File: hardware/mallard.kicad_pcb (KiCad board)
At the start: 4 copper layers, 101.6 x 101.6 mm, 75 parts, among them J1 USB_A, J2 Conn_02x03_Odd_Even, J3 Conn_01x03, SW1 RESET Switch, U1 TMP235, U10 LTC1983ES6-3, U11 STM32L4Q5xx, U2 TMP235, U3 TMP235, U4 BQ24210DQCT, U5 TMUX1309, U6 TMUX1309, U7 LMP7721, U8 TPS71710DRVR, U9 LMV554

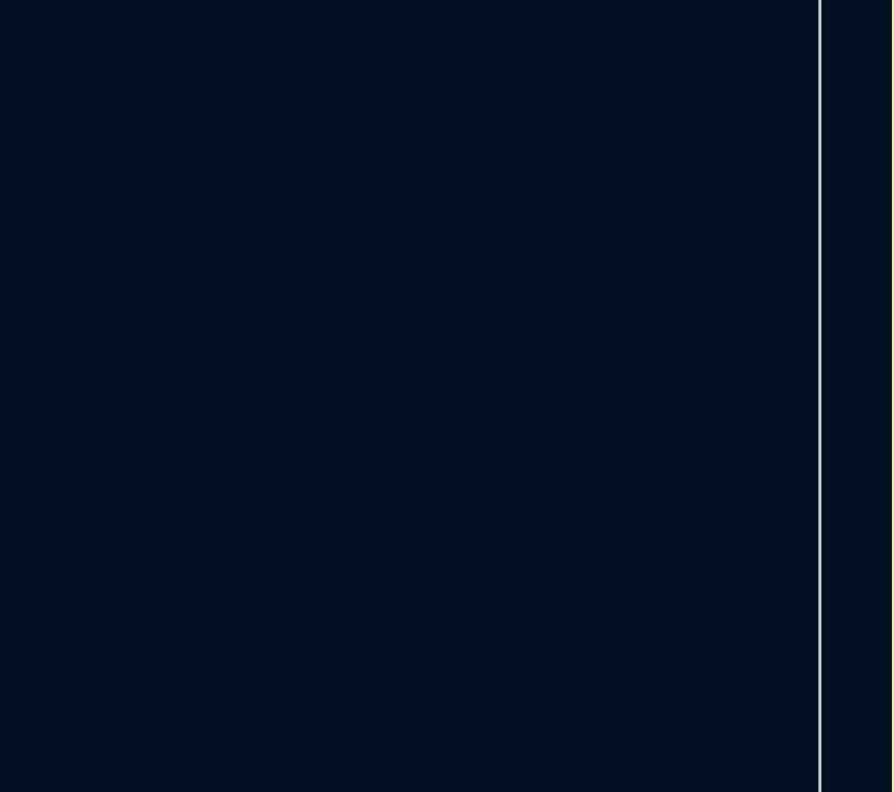
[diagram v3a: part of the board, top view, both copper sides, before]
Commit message: Modified footprints and added items to BOM
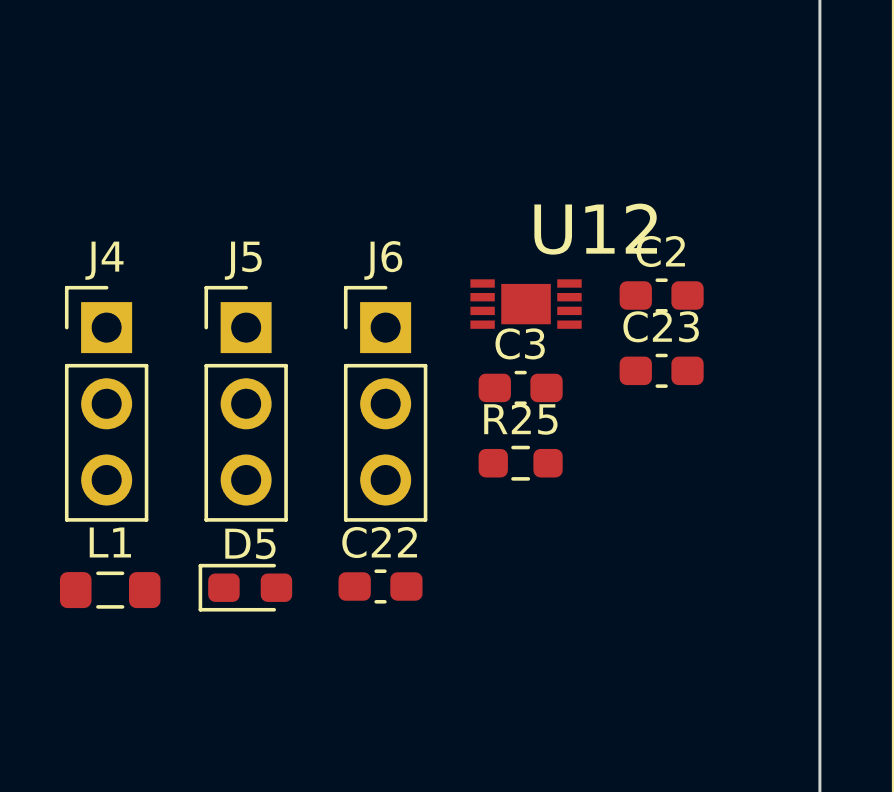
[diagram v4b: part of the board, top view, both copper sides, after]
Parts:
- added C2: 1uF, Capacitor_SMD:C_0603_1608Metric_Pad1.08x0.95mm_HandSolder, F.Cu at (34.9, 78.7)
- added C22: 3.3uF, Capacitor_SMD:C_0603_1608Metric_Pad1.08x0.95mm_HandSolder, F.Cu at (25.6, 88.4)
- added C23: 10uF, Capacitor_SMD:C_0603_1608Metric_Pad1.08x0.95mm_HandSolder, F.Cu at (34.9, 81.2)
- added C3: 1uF, Capacitor_SMD:C_0603_1608Metric_Pad1.08x0.95mm_HandSolder, F.Cu at (30.2, 81.8)
- added D5: RED, LED_SMD:LED_0603_1608Metric_Pad1.05x0.95mm_HandSolder, F.Cu at (21.2, 88.5)
- added J4: Conn_01x03, Connector_PinHeader_2.54mm:PinHeader_1x03_P2.54mm_Vertical, F.Cu at (16.4, 79.8)
- added J5: Conn_01x03, Connector_PinHeader_2.54mm:PinHeader_1x03_P2.54mm_Vertical, F.Cu at (21.1, 79.8)
- added J6: Conn_01x03, Connector_PinHeader_2.54mm:PinHeader_1x03_P2.54mm_Vertical, F.Cu at (25.7, 79.8)
- added L1: 4.7uH, Inductor_SMD:L_0805_2012Metric_Pad1.05x1.20mm_HandSolder, F.Cu at (16.5, 88.6)
- added R25: 370, Resistor_SMD:R_0603_1608Metric_Pad0.98x0.95mm_HandSolder, F.Cu at (30.2, 84.3)
- added U12: LTC3529EDCB, mallard:DFN200X300X80-9N, F.Cu at (30.4, 79.0)
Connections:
- U1 pad 2: GND -> Net-(U1-Pad2)
- U1 pad 4: +3V3 -> Net-(U1-Pad4)
- U11 pad 26: Net-(U11-Pad26) -> 5V_RST
- U11 pad 27: Net-(U11-Pad27) -> 5V_SHDN_L
- U11 pad 28: Net-(U11-Pad28) -> -3V3_SHDN_L
- U2 pad 2: GND -> Net-(U2-Pad2)
- U2 pad 4: +3V3 -> Net-(U2-Pad4)
- U3 pad 2: GND -> Net-(U3-Pad2)
- U3 pad 4: +3V3 -> Net-(U3-Pad4)
- U6 pad 12: Net-(U1-Pad3) -> Net-(J4-Pad2)
- U6 pad 14: Net-(U2-Pad3) -> Net-(J5-Pad2)
- U6 pad 15: Net-(U3-Pad3) -> Net-(J6-Pad2)

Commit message: Schematic and Layout Finished
Needs review
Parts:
- removed the C2 at (34.9, 78.7)
- removed the C2 at (114.8, 28.3)
- removed the C3 at (30.2, 81.8)
- removed D4: Orange, Resistor_SMD:R_0805_2012Metric_Pad1.20x1.40mm_HandSolder
- removed R10, R19: 20k, Resistor_SMD:R_0201_0603Metric_Pad0.64x0.40mm_HandSolder
- removed R13, R17, R24, R4, R6, R8: 10k, Resistor_SMD:R_0201_0603Metric_Pad0.64x0.40mm_HandSolder
- removed R14: 1k, Resistor_SMD:R_0201_0603Metric_Pad0.64x0.40mm_HandSolder
- removed R15: 30k, Resistor_SMD:R_0201_0603Metric_Pad0.64x0.40mm_HandSolder
- removed R16: 20k DNI, Resistor_SMD:R_0201_0603Metric_Pad0.64x0.40mm_HandSolder
- removed R18: 9.1k, Resistor_SMD:R_0201_0603Metric_Pad0.64x0.40mm_HandSolder
- removed R23: 680, Resistor_SMD:R_0603_1608Metric_Pad0.98x0.95mm_HandSolder
- removed U1, U2, U3: TMP235, Connector_PinHeader_2.54mm:PinHeader_1x05_P2.54mm_Vertical
- added C2: 1uF, Capacitor_SMD:C_0603_1608Metric_Pad1.08x0.95mm_HandSolder, F.Cu at (117.8, 38.1)
- moved J4 113.8 mm to (121.9, 37.2), turned to 90 degrees
- moved J5 96.4 mm to (107.5, 37.0), turned to 90 degrees
- moved J6 78.2 mm to (91.1, 36.9), turned to 90 degrees
- moved D5 73.7 mm to (88.8, 118.0), turned to 180 degrees
- moved L1 72.3 mm to (83.6, 115.7), turned to 180 degrees
- moved R25 71.4 mm to (91.2, 121.5), turned to 90 degrees
- moved C22 70.8 mm to (88.1, 121.6), turned to 270 degrees
- moved U12 67.9 mm to (83.4, 121.5)
- moved C23 59.7 mm to (79.0, 121.5), turned to 270 degrees
- moved C20 36.1 mm to (117.4, 101.0), turned to 0 degrees
- moved C19 29.3 mm to (112.2, 106.6)
- moved C18 25.8 mm to (109.8, 110.2)
- moved C3 11.6 mm to (103.2, 37.8), turned to 270 degrees
- moved C17 11.5 mm to (97.2, 107.8)
- moved C1 11.0 mm to (86.5, 37.6), turned to 270 degrees
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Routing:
- net MUX2_A1: track 0.00 -> 46.9 mm, vias 0 -> 2
- net -3V3_SHDN_L: track 0.00 -> 46.5 mm, vias 0 -> 4
- net /RESET_L: track 0.00 -> 46.4 mm
- net MUX2_A0: track 0.00 -> 45.4 mm, vias 0 -> 2
- net Charge_EN: track 1.38 -> 46.5 mm, vias 1 -> 2
- net Moisture_Sense: track 2.16 -> 46.9 mm, vias 0 -> 4
- net /SWDIO: track 0.00 -> 43.9 mm, vias 0 -> 2
- net /SWCLK: track 0.00 -> 42.2 mm, vias 0 -> 2
- net +1V0_EN: track 0.00 -> 42.0 mm, vias 0 -> 2
- net +3V3: track 37.9 -> 79.2 mm, vias 85 -> 90
- net MUX1_A1: track 0.00 -> 40.6 mm, vias 0 -> 2
- net MUX1_A0: track 0.00 -> 40.3 mm, vias 0 -> 2
- net USART1_TX: track 0.00 -> 40.0 mm, vias 0 -> 2
- net MUX1_EN: track 0.00 -> 39.3 mm, vias 0 -> 2
- net MUX2_EN: track 0.00 -> 38.9 mm, vias 0 -> 2
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- added copper zone on F.Cu, net +5V
- added copper zone on Power, net +5V

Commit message: Updated footprints
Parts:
- added C2: 1uF, Capacitor_SMD:C_0603_1608Metric_Pad1.08x0.95mm_HandSolder, F.Cu at (54.0, 20.3)
- added C3: 1uF, Capacitor_SMD:C_0603_1608Metric_Pad1.08x0.95mm_HandSolder, F.Cu at (58.8, 17.4)
- added D4: Orange, Diode_SMD:D_0805_2012Metric_Castellated, F.Cu at (54.2, 17.6)
- added R10: 20k, Resistor_SMD:R_0603_1608Metric_Pad0.98x0.95mm_HandSolder, F.Cu at (54.0, 25.3)
- added R13: 10k, Resistor_SMD:R_0603_1608Metric_Pad0.98x0.95mm_HandSolder, F.Cu at (58.3, 22.8)
- added R14: 1k, Resistor_SMD:R_0603_1608Metric_Pad0.98x0.95mm_HandSolder, F.Cu at (62.7, 19.9)
- added R15: 30k, Resistor_SMD:R_0603_1608Metric_Pad0.98x0.95mm_HandSolder, F.Cu at (67.5, 17.4)
- added R16: 20k DNI, Resistor_SMD:R_0603_1608Metric_Pad0.98x0.95mm_HandSolder, F.Cu at (58.3, 25.3)
- added R17: 10k, Resistor_SMD:R_0603_1608Metric_Pad0.98x0.95mm_HandSolder, F.Cu at (62.7, 22.4)
- added R18: 9.1k, Resistor_SMD:R_0603_1608Metric_Pad0.98x0.95mm_HandSolder, F.Cu at (67.0, 19.9)
- added R19: 20k, Resistor_SMD:R_0603_1608Metric_Pad0.98x0.95mm_HandSolder, F.Cu at (62.7, 24.9)
- added R23: 680, Resistor_SMD:R_0603_1608Metric_Pad0.98x0.95mm_HandSolder, F.Cu at (67.0, 22.4)
- added R24: 10k, Resistor_SMD:R_0603_1608Metric_Pad0.98x0.95mm_HandSolder, F.Cu at (67.0, 24.9)
- added R4: 10k, Resistor_SMD:R_0603_1608Metric_Pad0.98x0.95mm_HandSolder, F.Cu at (54.0, 22.8)
- added R6: 10k, Resistor_SMD:R_0603_1608Metric_Pad0.98x0.95mm_HandSolder, F.Cu at (58.3, 20.3)
- added R8: 10k, Resistor_SMD:R_0603_1608Metric_Pad0.98x0.95mm_HandSolder, F.Cu at (63.2, 17.4)

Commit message: Finished schematic and layout
Needs review
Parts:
- removed the C2 at (54.0, 20.3)
- removed the C3 at (58.8, 17.4)
- moved D4 106.5 mm to (104.0, 111.7), turned to 270 degrees
- moved R24 104.9 mm to (132.4, 106.8), turned to 270 degrees
- moved R23 95.5 mm to (101.2, 111.6), turned to 270 degrees
- moved R15 93.1 mm to (129.7, 86.7), turned to 270 degrees
- moved R16 91.5 mm to (126.2, 86.7), turned to 90 degrees
- moved R14 86.6 mm to (117.8, 86.7), turned to 270 degrees
- moved R17 86.5 mm to (120.5, 86.7), turned to 90 degrees
- moved R13 84.0 mm to (112.9, 86.7), turned to 270 degrees
- moved R18 82.4 mm to (115.3, 86.7), turned to 90 degrees
- moved R10 80.0 mm to (106.7, 85.6), turned to 180 degrees
- moved R19 78.1 mm to (110.5, 86.7), turned to 270 degrees
- moved R8 77.2 mm to (99.5, 85.5), turned to 180 degrees
- moved R6 64.4 mm to (101.5, 68.2), turned to 270 degrees
- moved R4 63.9 mm to (99.0, 68.2), turned to 90 degrees
- moved C5 10.7 mm to (91.7, 57.1)
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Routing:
- net Eh_Sense: track 30.1 -> 41.4 mm, vias 0 -> 2
- net Net-(D4-Pad1): track 0.00 -> 4.77 mm
- net Net-(R10-Pad1): track 29.9 -> 34.7 mm
- net Net-(R16-Pad1): track 7.52 -> 12.2 mm
- net Net-(R13-Pad2): track 12.3 -> 16.7 mm
- net Temp_Sense: track 33.5 -> 29.4 mm, vias 3 -> 5
- net /USB+: track 26.5 -> 30.5 mm, vias 2 -> 1
- net Net-(R4-Pad1): track 6.41 -> 10.1 mm
- net Net-(R10-Pad2): track 12.0 -> 15.3 mm
- net Net-(D4-Pad2): track 0.00 -> 2.90 mm
- net -3V3_SHDN_L: track 46.5 -> 48.3 mm, vias 4 -> 2
- net Net-(R17-Pad2): track 33.3 -> 35.0 mm
- net GND: track 69.3 -> 70.6 mm
- net Ref_Out: track 5.80 -> 6.97 mm
- net Net-(R4-Pad2): track 9.95 -> 8.83 mm
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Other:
- net class Default: clearance 0.2 -> 0.1524
- rule trace_clearance: 0.2 -> 0.1524

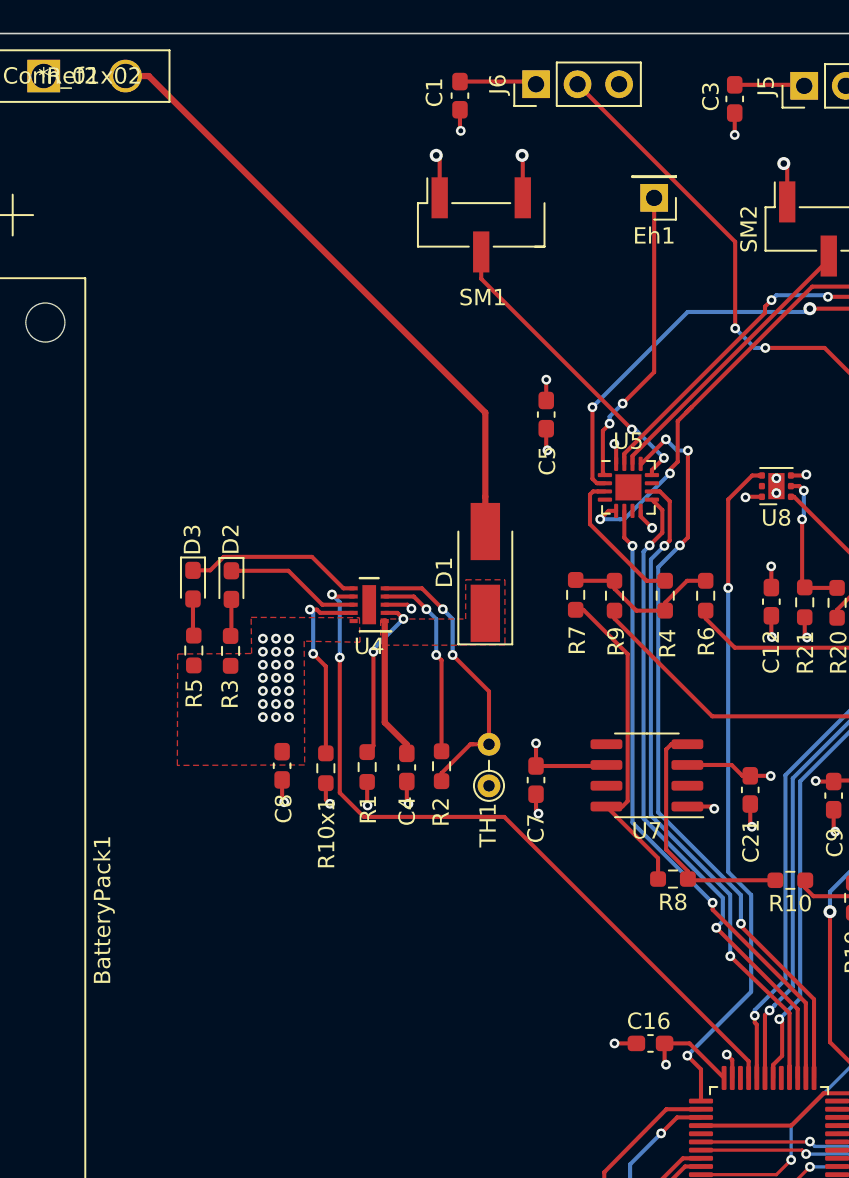
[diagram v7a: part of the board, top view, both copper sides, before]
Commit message: Small layout changes
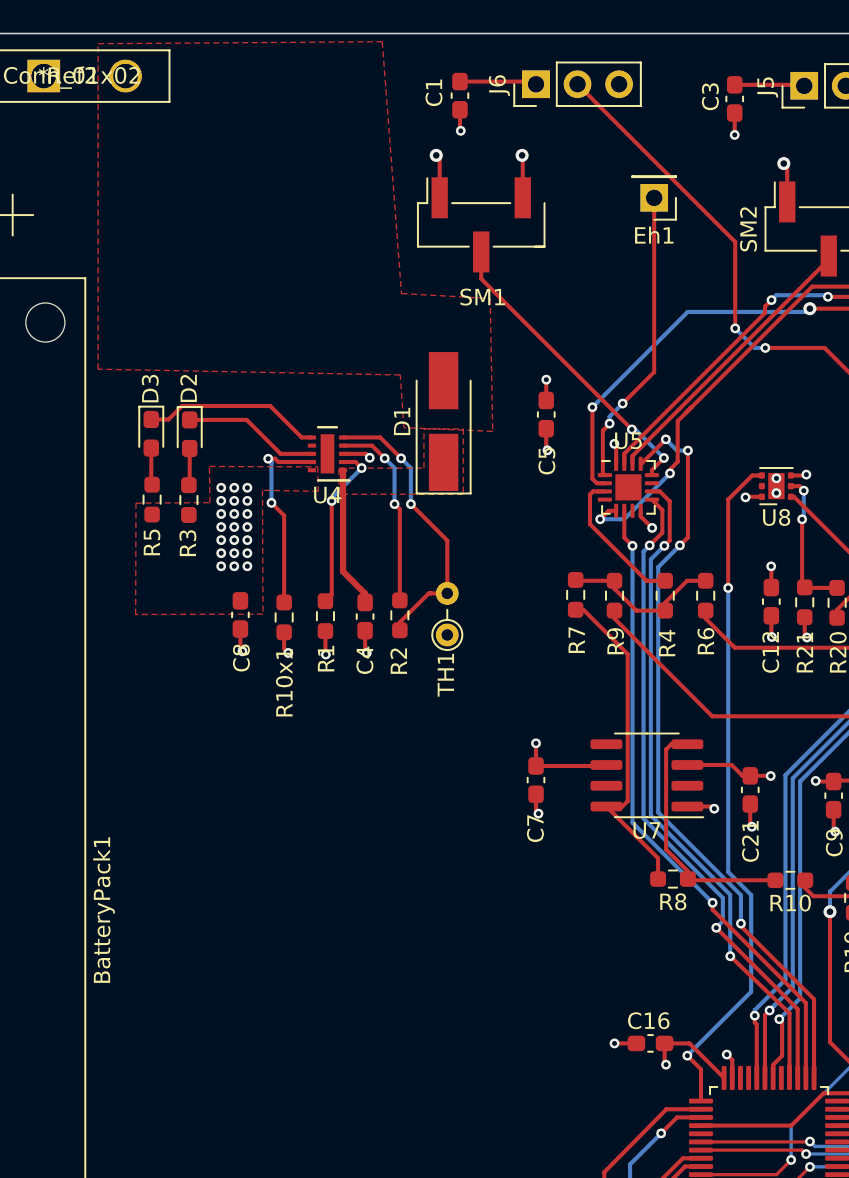
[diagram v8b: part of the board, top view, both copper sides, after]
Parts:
- moved R1 9.57 mm to (78.2, 69.4)
- moved C8 9.57 mm to (73.0, 69.3)
- moved D2 9.57 mm to (69.9, 58.3)
- moved R5 9.57 mm to (67.6, 62.3)
- moved D1 9.57 mm to (85.5, 57.5)
- moved D3 9.57 mm to (67.6, 58.3)
- moved U4 9.57 mm to (78.3, 59.5)
- moved C4 9.57 mm to (80.7, 69.5)
- moved R10x1 9.57 mm to (75.7, 69.5)
- moved R2 9.57 mm to (82.8, 69.4)
- moved R3 9.57 mm to (69.9, 62.3)
- moved TH1 9.57 mm to (85.7, 70.6)
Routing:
- net Charge_EN: track 46.5 -> 0.00 mm, vias 2 -> 0
- net Net-(D1-Pad2): track 37.8 -> 0.00 mm
- added copper zone on F.Cu, net Net-(D1-Pad2)
